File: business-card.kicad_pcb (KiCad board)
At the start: 2 copper layers, 45 parts, among them J1 Conn_02x04_Counter_Clockwise, J3 USB_B, Q1 Q_NMOS_GSD, SW1 SW_Push, U4 JW5211, U5 JW5211, U6 JW5211, U7 F1C100s, U8 AT25SF081-SSHD-X, Y1 24MHz

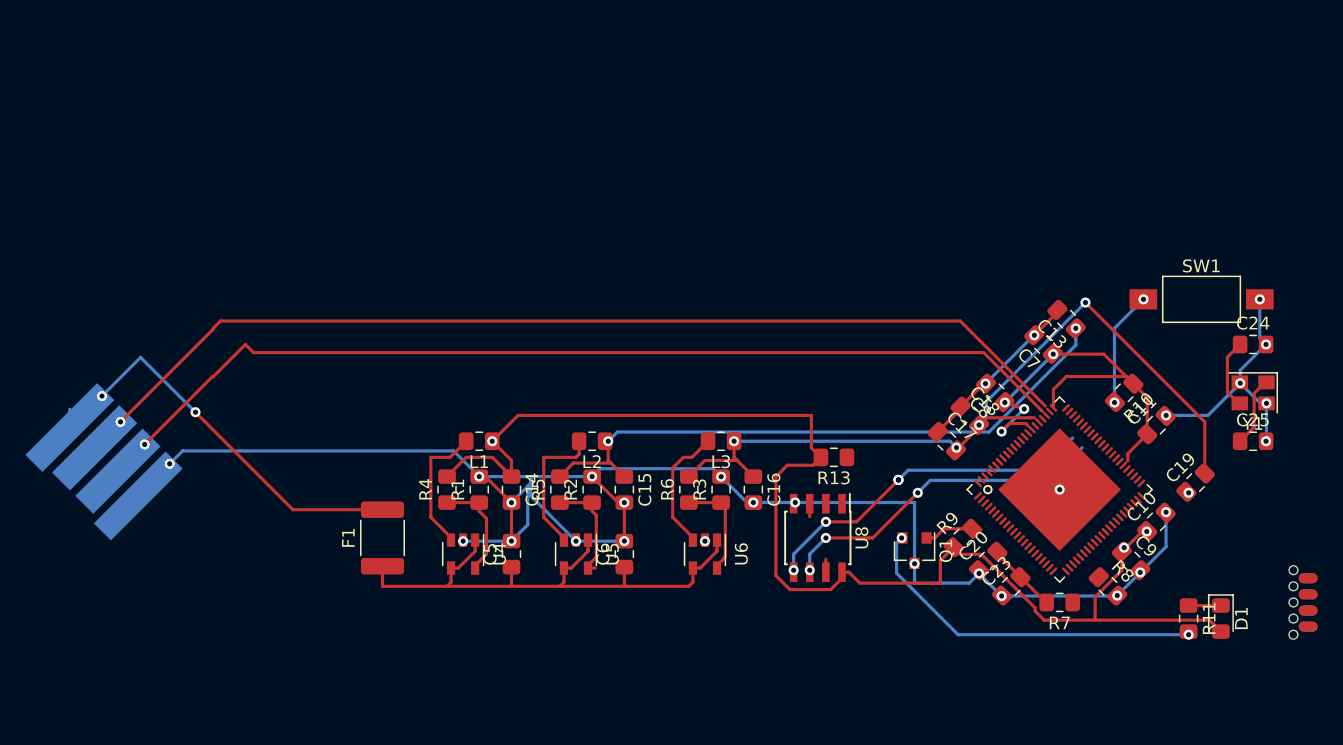
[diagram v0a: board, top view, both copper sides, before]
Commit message: Remove traces to try autoroute
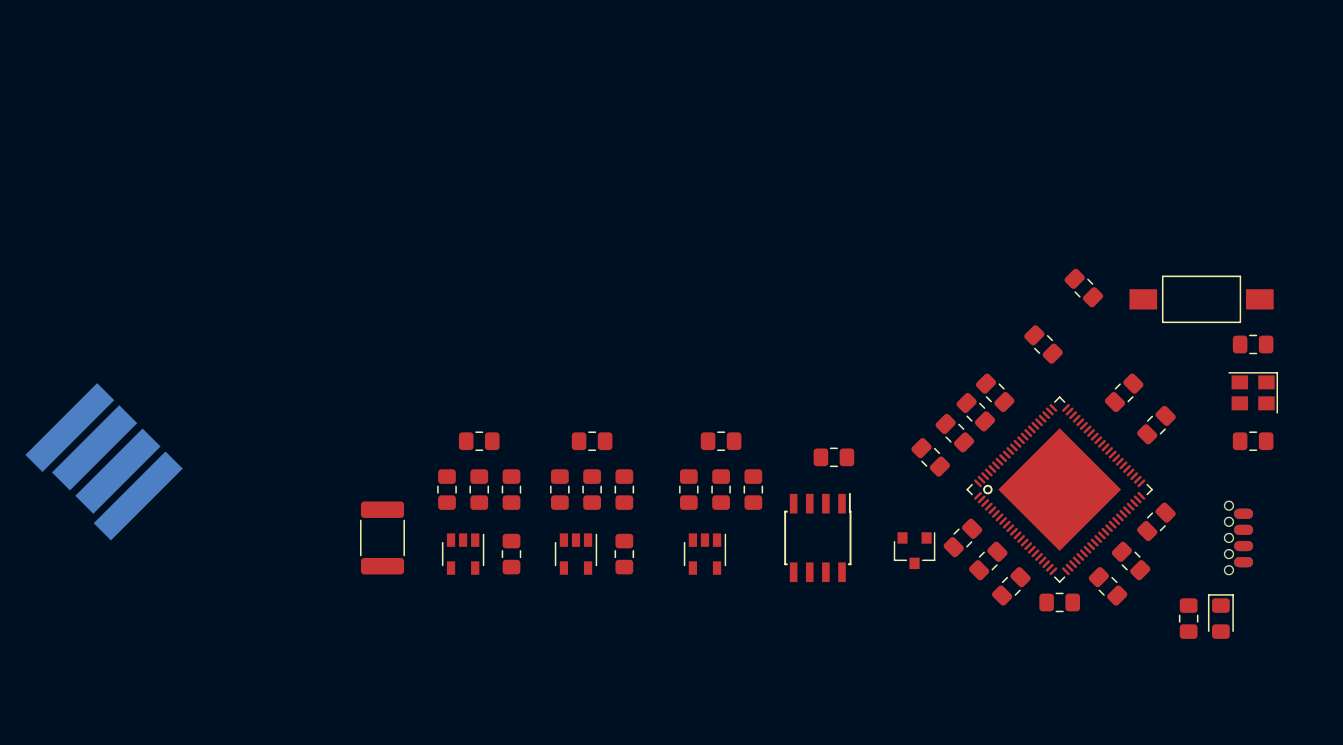
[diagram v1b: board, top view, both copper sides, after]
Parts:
- moved C19 18.2 mm to (111.5, 104.4), turned to 315 degrees
- moved J1 7.18 mm to (133.3, 114.3)
- moved C13 2.80 mm to (120.0, 94.6)
- moved C18 1.80 mm to (109.9, 106.0)
- moved C17 1.80 mm to (108.0, 108.0)
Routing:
- net GND: track 162.2 -> 0.00 mm, vias 29 -> 0
- net +3V3: track 137.0 -> 0.00 mm, vias 7 -> 0
- net /USB_DN: track 81.8 -> 0.00 mm, vias 1 -> 0
- net /USB_DP: track 79.1 -> 0.00 mm, vias 1 -> 0
- net +1V1: track 63.3 -> 0.00 mm, vias 4 -> 0
- net +2V5: track 54.7 -> 0.00 mm, vias 2 -> 0
- net /FUSE_PWR: track 43.4 -> 0.00 mm
- net /USB_VBUS: track 29.8 -> 0.00 mm, vias 2 -> 0
- net Net-(Q1-Pad2): track 28.0 -> 0.00 mm, vias 2 -> 0
- net /SPI_MOSI: track 27.0 -> 0.00 mm, vias 4 -> 0
- net /SPI_CLK: track 26.2 -> 0.00 mm, vias 3 -> 0
- net Net-(L2-Pad2): track 11.1 -> 0.00 mm
- net Net-(L1-Pad2): track 10.5 -> 0.00 mm
- net Net-(L3-Pad2): track 10.00 -> 0.00 mm
- net /RESET: track 9.07 -> 0.00 mm, vias 2 -> 0
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
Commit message: cleanup
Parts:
- J1: moved to F.Cu
- moved C13 20.0 mm to (127.2, 113.3), turned to 315 degrees
- moved C8 17.2 mm to (115.3, 119.9), turned to 225 degrees
- moved C10 17.0 mm to (108.7, 113.0), turned to 135 degrees
- moved C20 12.8 mm to (125.2, 115.3), turned to 135 degrees
- moved C7 12.2 mm to (108.5, 108.0)
- moved C9 10.6 mm to (113.3, 117.9), turned to 225 degrees
- moved C23 9.20 mm to (123.4, 117.1), turned to 135 degrees
- moved SW1 5.24 mm to (124.5, 97.5)
- moved C19 3.97 mm to (114.6, 101.9)
- moved J1 2.84 mm to (134.6, 111.8), turned to 90 degrees
- moved R7 2.65 mm to (118.9, 121.9), turned to 0 degrees
- moved C17 2.54 mm to (110.0, 106.4)
- moved R10 2.17 mm to (121.2, 102.1), turned to 315 degrees
- moved R11 2.09 mm to (126.2, 121.2)
- moved C18 2.01 mm to (111.5, 104.9)
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
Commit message: Complete board.
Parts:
- moved J3 20.4 mm to (54.5, 125.5), turned to 150 degrees
- moved C13 19.8 mm to (108.2, 107.8), turned to 135 degrees
- moved C23 19.0 mm to (115.3, 100.0), turned to 315 degrees
- moved C18 17.0 mm to (125.0, 115.3), turned to 45 degrees
- moved C17 14.0 mm to (115.0, 119.5), turned to 45 degrees
- moved C8 8.09 mm to (123.2, 118.2), turned to 135 degrees
- moved R11 5.08 mm to (131.3, 121.2)
- moved C20 3.06 mm to (127.8, 113.8)
- moved C7 3.03 mm to (110.4, 105.6)
- moved C10 2.90 mm to (106.3, 111.3)
- moved C19 2.63 mm to (112.5, 103.5)
- moved C11 2.54 mm to (127.3, 103.5)
- moved F1 2.31 mm to (65.0, 112.0)
- moved R10 2.15 mm to (119.3, 101.0), turned to 135 degrees
- moved L3 1.56 mm to (93.0, 106.8)
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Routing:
- net +3V3: track 0.00 -> 143.3 mm, vias 0 -> 4
- net +2V5: track 0.00 -> 95.2 mm, vias 0 -> 10
- net /USB_DP: track 0.00 -> 75.9 mm, vias 0 -> 1
- net /USB_DN: track 0.00 -> 75.6 mm, vias 0 -> 1
- net +1V1: track 0.00 -> 72.2 mm, vias 0 -> 6
- net /SPI_CLK: track 0.00 -> 55.0 mm, vias 0 -> 2
- net GND: track 0.00 -> 54.4 mm, vias 0 -> 28
- net /SPI_MOSI: track 0.00 -> 52.3 mm, vias 0 -> 2
- net /RESET: track 0.00 -> 44.0 mm, vias 0 -> 2
- net /SPI_MISO: track 0.00 -> 43.0 mm, vias 0 -> 3
- net /SPI_CS: track 0.00 -> 43.0 mm, vias 0 -> 3
- net /FUSE_PWR: track 0.00 -> 38.8 mm
- net Net-(Q1-Pad2): track 0.00 -> 34.0 mm
- net /CLKN: track 0.00 -> 16.6 mm
- net /USB_VBUS: track 0.00 -> 16.5 mm, vias 0 -> 1
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- added copper zone on B.Cu, net GND
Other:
- rule trace_min: 0.2 -> 0.137

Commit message: images.
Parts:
- C7: footprint Capacitor_SMD:C_0805_2012Metric_Pad1.15x1.40mm_HandSolder -> Capacitor_SMD:C_0805_2012Metric_Pad1.18x1.45mm_HandSolder
- F1: footprint Fuse:Fuse_1812_4532Metric_Pad1.30x3.40mm_HandSolder -> Fuse:Fuse_0805_2012Metric
- moved C7 8.40 mm to (109.3, 114.0), turned to 225 degrees
- moved F1 3.34 mm to (67.1, 114.6)
- moved R13 0.13 mm to (100.0, 109.0)
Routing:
- net GND: track 54.4 -> 106.4 mm, vias 28 -> 24
- net +3V3: track 143.3 -> 138.4 mm
- net +2V5: track 95.2 -> 90.9 mm
- net /USB_DP: track 75.9 -> 72.4 mm
- net /FUSE_PWR: track 38.8 -> 36.2 mm
- net /USB_VBUS: track 16.5 -> 14.3 mm
- net /SPI_MISO: track 43.0 -> 44.7 mm
- net /STATUS: track 9.48 -> 9.85 mm, vias 0 -> 2
- net Net-(U8-Pad3): track 5.60 -> 5.93 mm, vias 2 -> 0
- net /SPI_CS: track 43.0 -> 43.1 mm, vias 3 -> 4
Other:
- board outline added: 90 x 54.5 mm

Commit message: rev 1
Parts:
- added G***: LOGO, business-card:copyleft, B.Cu at (126.5, 94.0)
- added G***: LOGO, business-card:copyleft, F.Cu at (63.8, 105.0)
- added G***: LOGO, business-card:logo, F.Cu at (91.0, 96.8)
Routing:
- net GND: track 106.4 -> 95.6 mm, vias 24 -> 26
- net /USB_VBUS: track 14.3 -> 20.9 mm
- net /USB_DP: track 72.4 -> 77.3 mm
- net /USB_DN: track 76.0 -> 78.6 mm
- net +3V3: track 138.4 -> 137.4 mm
- net /CLKN: track 16.6 -> 17.2 mm
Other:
- board text added: "JLCJLCJLCJLC"
- board text added: "RESET"

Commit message: rev1 update
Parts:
- moved G*** 11.1 mm to (90.9, 85.6)
- moved G*** 0.35 mm to (126.4, 93.7)
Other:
- rule pad_to_mask_clearance: 0.051 -> 0

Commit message: reorg
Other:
- net class Default removed
